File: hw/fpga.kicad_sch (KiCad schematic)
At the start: 34 parts, among them U3 ICE40UL1K-CM36AITR

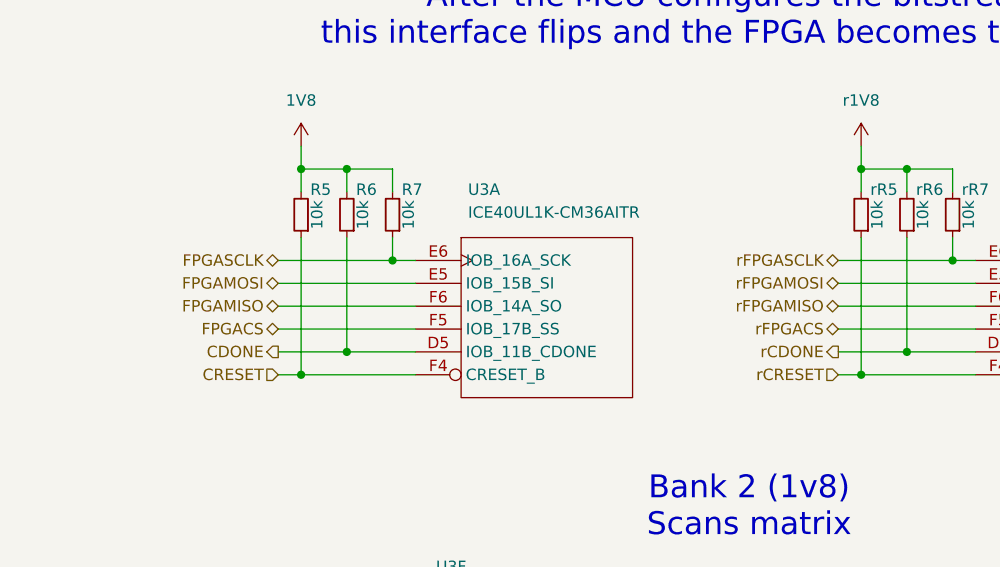
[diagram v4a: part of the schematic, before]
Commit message: Hook up mcu
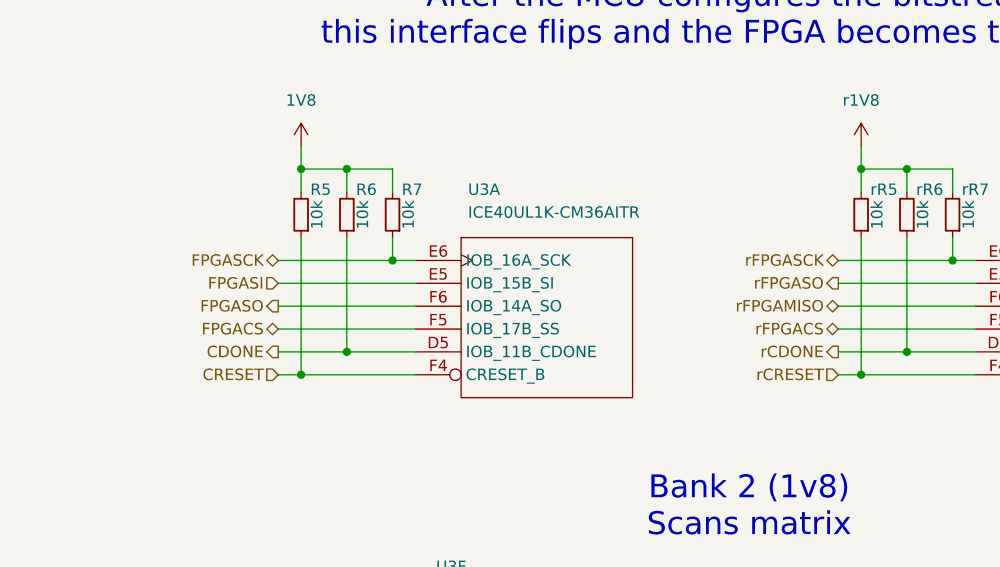
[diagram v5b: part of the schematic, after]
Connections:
- net FPGAMISO renamed FPGASO
- net FPGAMOSI renamed FPGASI
- net FPGASCLK renamed FPGASCK
- net rFPGAMOSI renamed rFPGASO
- net rFPGASCLK renamed rFPGASCK
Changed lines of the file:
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@@
 		)
 	)
-	(hierarchical_label "rFPGAMOSI"
-		(shape bidirectional)
+	(hierarchical_label "rFPGASO"
+		(shape output)
 		(at 232.41 53.34 180)
 		(effects
@@
 		)
 	)
-	(hierarchical_label "FPGAMISO"
-		(shape bidirectional)
+	(hierarchical_label "FPGASO"
+		(shape output)
 		(at 170.18 55.88 180)
 		(effects
@@
 		)
 	)
-	(hierarchical_label "FPGASCLK"
+	(hierarchical_label "FPGASCK"
 		(shape bidirectional)
 		(at 170.18 50.8 180)
@@
 		)
 	)
-	(hierarchical_label "rFPGASCLK"
+	(hierarchical_label "rFPGASCK"
 		(shape bidirectional)
 		(at 232.41 50.8 180)
@@
 		)
 	)
-	(hierarchical_label "FPGAMOSI"
-		(shape bidirectional)
+	(hierarchical_label "FPGASI"
+		(shape input)
 		(at 170.18 53.34 180)
 		(effects

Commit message: Sheet pins
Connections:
- net rFPGAMISO is gone; now on net rFPGASO: rU3.F6 (IOB_14A_SO)
- net rFPGASO: no longer rU3.E5 (IOB_15B_SI)
- new net rFPGASI: rU3.E5 (IOB_15B_SI)
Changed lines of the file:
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@@
 		)
 	)
-	(hierarchical_label "rFPGASO"
-		(shape output)
+	(hierarchical_label "rFPGASI"
+		(shape input)
 		(at 232.41 53.34 180)
 		(effects
@@
 		)
 	)
-	(hierarchical_label "rFPGAMISO"
-		(shape bidirectional)
+	(hierarchical_label "rFPGASO"
+		(shape output)
 		(at 232.41 55.88 180)
 		(effects

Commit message: Debug header
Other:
- title: (none) -> Alidade
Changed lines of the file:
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@@
 	(generator_version "9.0")
 	(paper "A4")
+	(title_block
+		(title "Alidade")
+		(date "2026-03-29")
+		(rev "1.0.0rc1")
+	)
 	(text "Power Sequencing\n1. VCC(PLL) @ 1V2 \n2. VCCIO(1,2) @ 1v8\n3. VCCIO0 and VPP2V5 @ 3V3 "
 		(exclude_from_sim no)
